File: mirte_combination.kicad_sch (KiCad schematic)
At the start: 46 parts, among them J1 Servo3, J10 IR1, J11 Conn_01x13_Female, J12 IR Object Detector 1, J14 IR2, J17 MC1, J18 MC2, J19 Servo1, J2 Conn_01x20_Female, J20 SRF1, J21 ENC2, J23 MC1-A, J24 MC1-B, J25 SRF2, J26 ENC1, J27 Servo2, J28 I2C2, J3 Servo4, J30 I2C1, J32 line out right, J33 line out left, J34 Power in, J35 Power out, J37 on/off, J4 Conn_01x20_Female, J5 MC2-A, J6 MC2-B, J7 Keypad, J8 Conn_01x06_Female, J9 IR Object Detector 2, Q1 DMG2305UX, Q2 DMN2050L, SW1 on/off, U1 CH340C, U2 CH340E

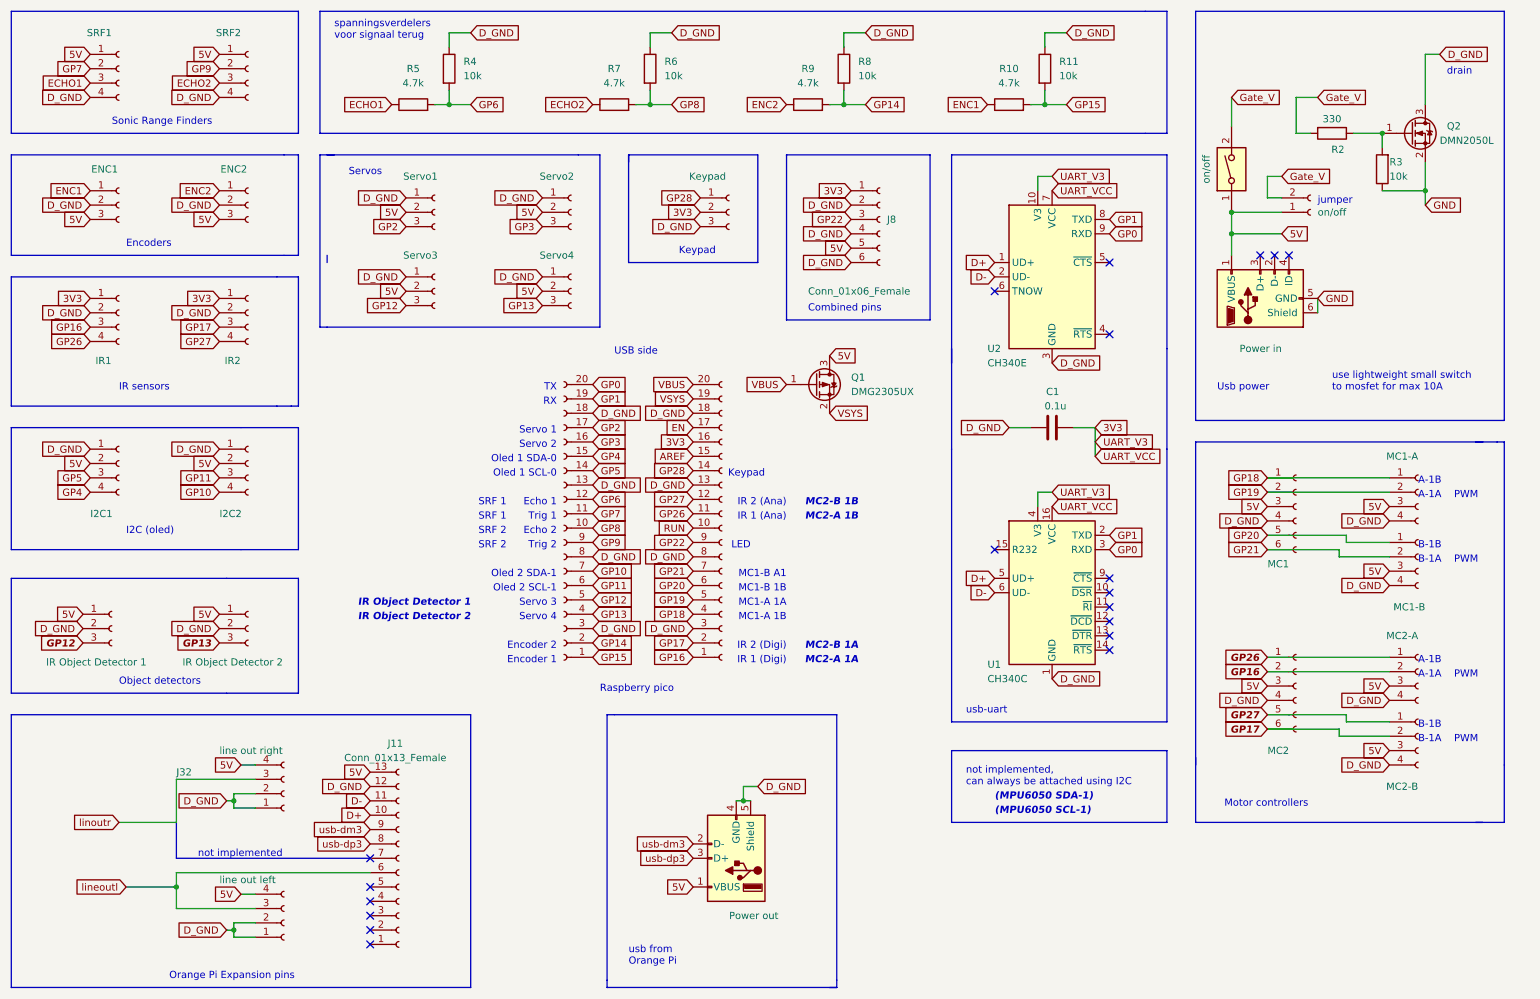
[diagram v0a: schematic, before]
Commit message: v0.7: swap encoder1/2<->servo1/2 for PWM fix
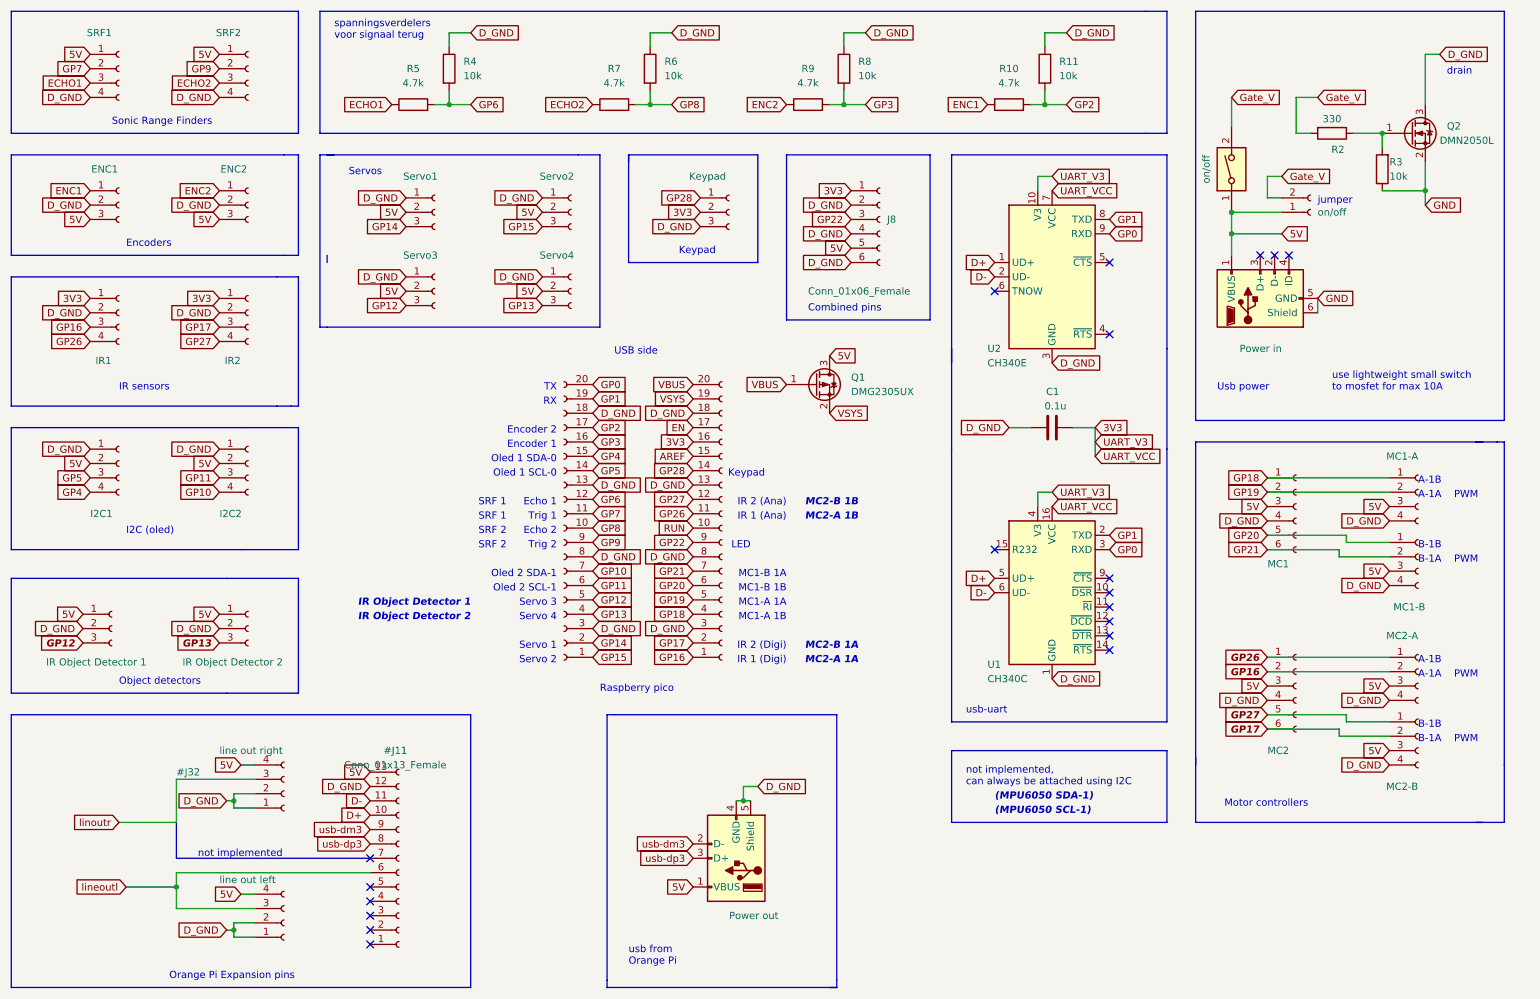
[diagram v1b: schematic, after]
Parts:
- renumbered J11 to #J11, J32 to #J32, J5 to #J5, J6 to #J6
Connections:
- net GP14: now also J19.3 (Pin_3); no longer R8.2, R9.2
- net GP15: now also J27.3 (Pin_3); no longer R10.2, R11.2
- net GP2: now also R10.2, R11.2; no longer J19.3 (Pin_3)
- net GP3: now also R8.2, R9.2; no longer J27.3 (Pin_3)
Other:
- note added: "MC1-B 1A"
- note removed: "MC1-B A1"

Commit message: adapted text, v0.8
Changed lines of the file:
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@@
   (title_block
     (date "2023-06-09")
-    (rev "0.7")
+    (rev "0.8")
   )
   (junction (at 233.68 53.34) (diameter 0) (color 0 0 0 0)
@@
     (effects (font (size 1.27 1.27)) (justify left bottom))
   )
-  (text "Encoder 1" (at 114.3 95.25 0)
+  (text "Encoder 2" (at 114.3 95.25 0)
     (effects (font (size 1.27 1.27)) (justify right bottom))
   )
@@
     (effects (font (size 1.27 1.27)) (justify right bottom))
   )
-  (text "Encoder 2" (at 114.3 92.71 0)
-    (effects (font (size 1.27 1.27)) (justify right bottom))
-  )
+  (text "Encoder 1" (at 114.3 92.71 0)
+    (effects (font (size 1.27 1.27)) (justify right bottom))
+  )
